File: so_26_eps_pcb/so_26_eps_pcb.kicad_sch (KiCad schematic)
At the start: 83 parts, among them J1 Conn_02x12_Odd_Even, SW1 SW_SPDT, U1 LM22679TJ-ADJ/NOPB, U2 LM22679TJ-ADJ/NOPB

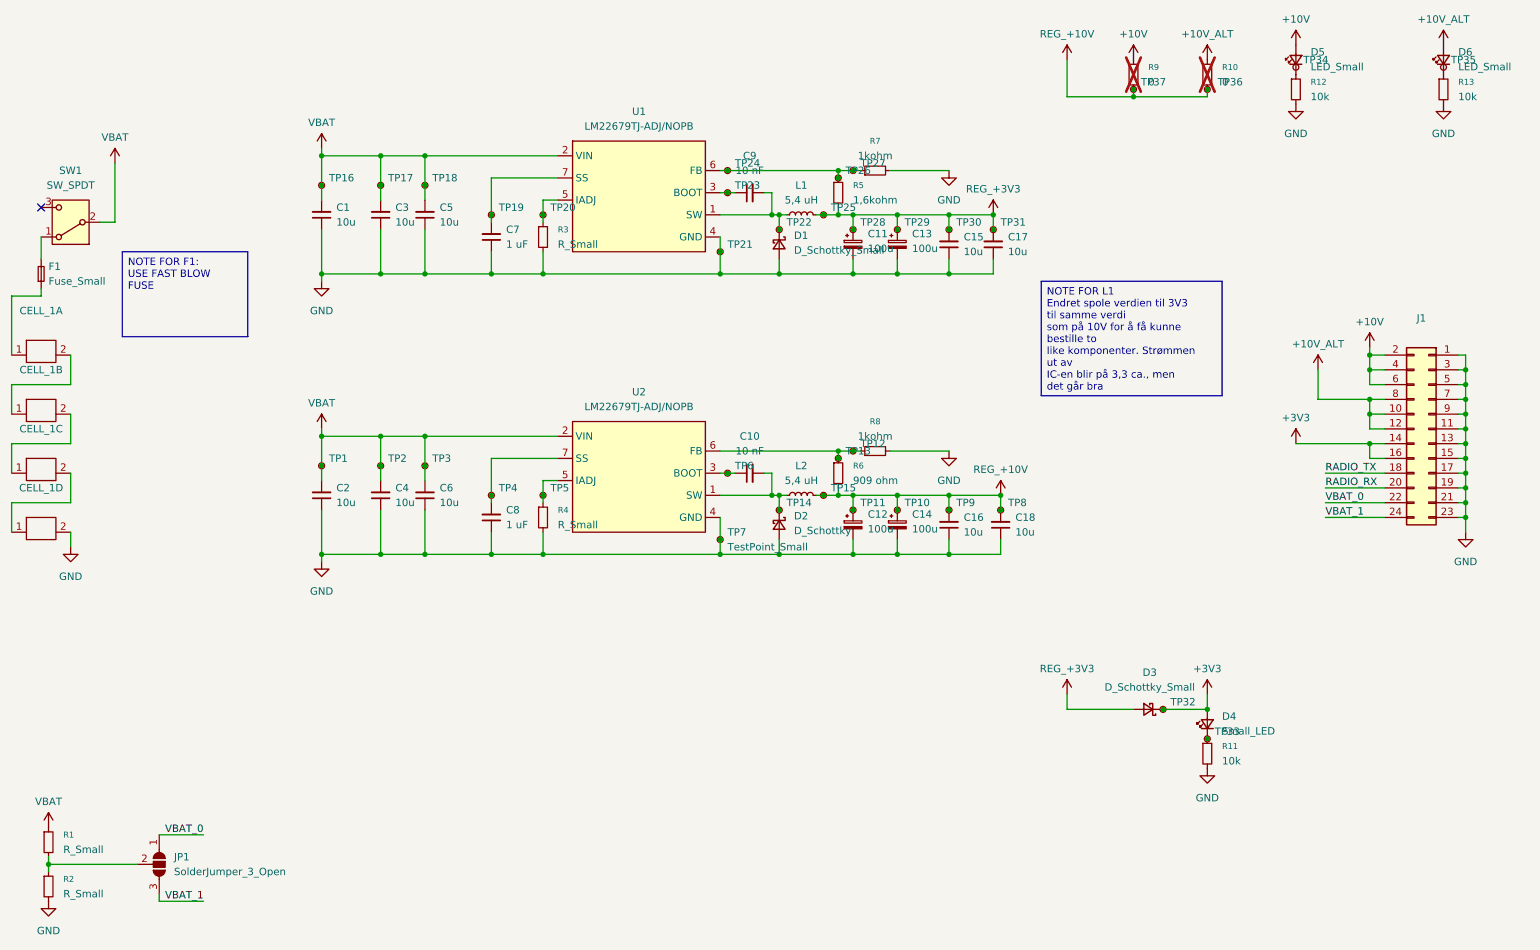
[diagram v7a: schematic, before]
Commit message: Changed battery cells
Gave input and outputs their own number
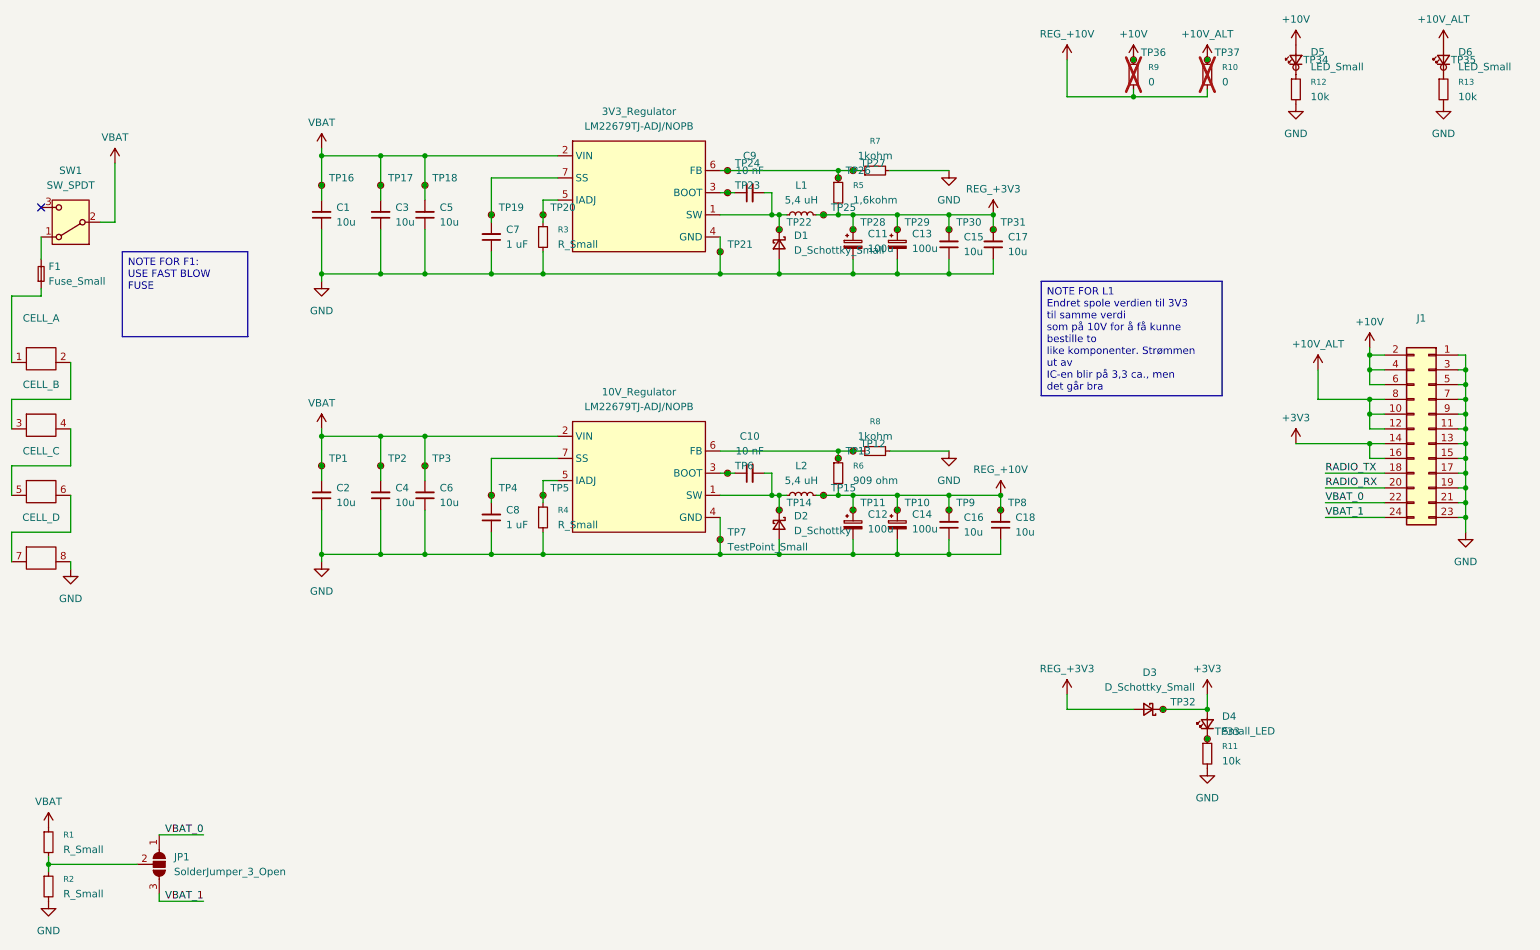
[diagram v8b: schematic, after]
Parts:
- removed CELL_1: ~, symbol MySymbols:Battery_18650_boxes
- added CELL_: ~, symbol MySymbols:Battery_18650_boxes
- TP1, TP10, TP11, TP12, TP13, TP14, TP15, TP16, TP17, TP18, TP19, TP2, TP20, TP21, TP22, TP23, TP24, TP25, TP26, TP27, TP28, TP29, TP3, TP30, TP31, TP32, TP33, TP34, TP35, TP36, TP37, TP4, TP5, TP6, TP7, TP8, TP9: footprint (none) -> TestPoint:TestPoint_Pad_D2.5mm
- renumbered U2 to 10V_Regulator, U1 to 3V3_Regulator
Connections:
- net +10V: now also TP36.1
- net +10V_ALT: now also TP37.1
- net GND: now also CELL_.8
- net REG_+10V: no longer TP36.1, TP37.1
- net at F1.1: now also CELL_.1
- new net: CELL_.6, CELL_.7
- new net: CELL_.4, CELL_.5
- new net: CELL_.2, CELL_.3
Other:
- moved on the sheet: TP37
